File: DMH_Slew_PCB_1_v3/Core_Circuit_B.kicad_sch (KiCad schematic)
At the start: 60 parts, among them J21 Conn_02x03_Top_Bottom, J22 Conn_02x06_Top_Bottom, J23 Conn_02x03_Top_Bottom, J24 Conn_02x03_Top_Bottom, J25 Conn_02x06_Top_Bottom, J26 Conn_02x03_Top_Bottom, J27 Conn_01x08, J28 Conn_01x08, J29 Conn_01x08, J30 Conn_01x08, J6 TS_Jack_6.35mm_Sw, J7 TS_Jack_6.35mm_Sw, J8 TS_Jack_6.35mm_Sw, Q10 BC558, Q7 BC548, Q8 BC548, Q9 BC558, SW4 SW_DPDT_3way, SW5 SW_DPDT, SW6 SPDT_OnOffOn, U3 TL074, U4 TL074

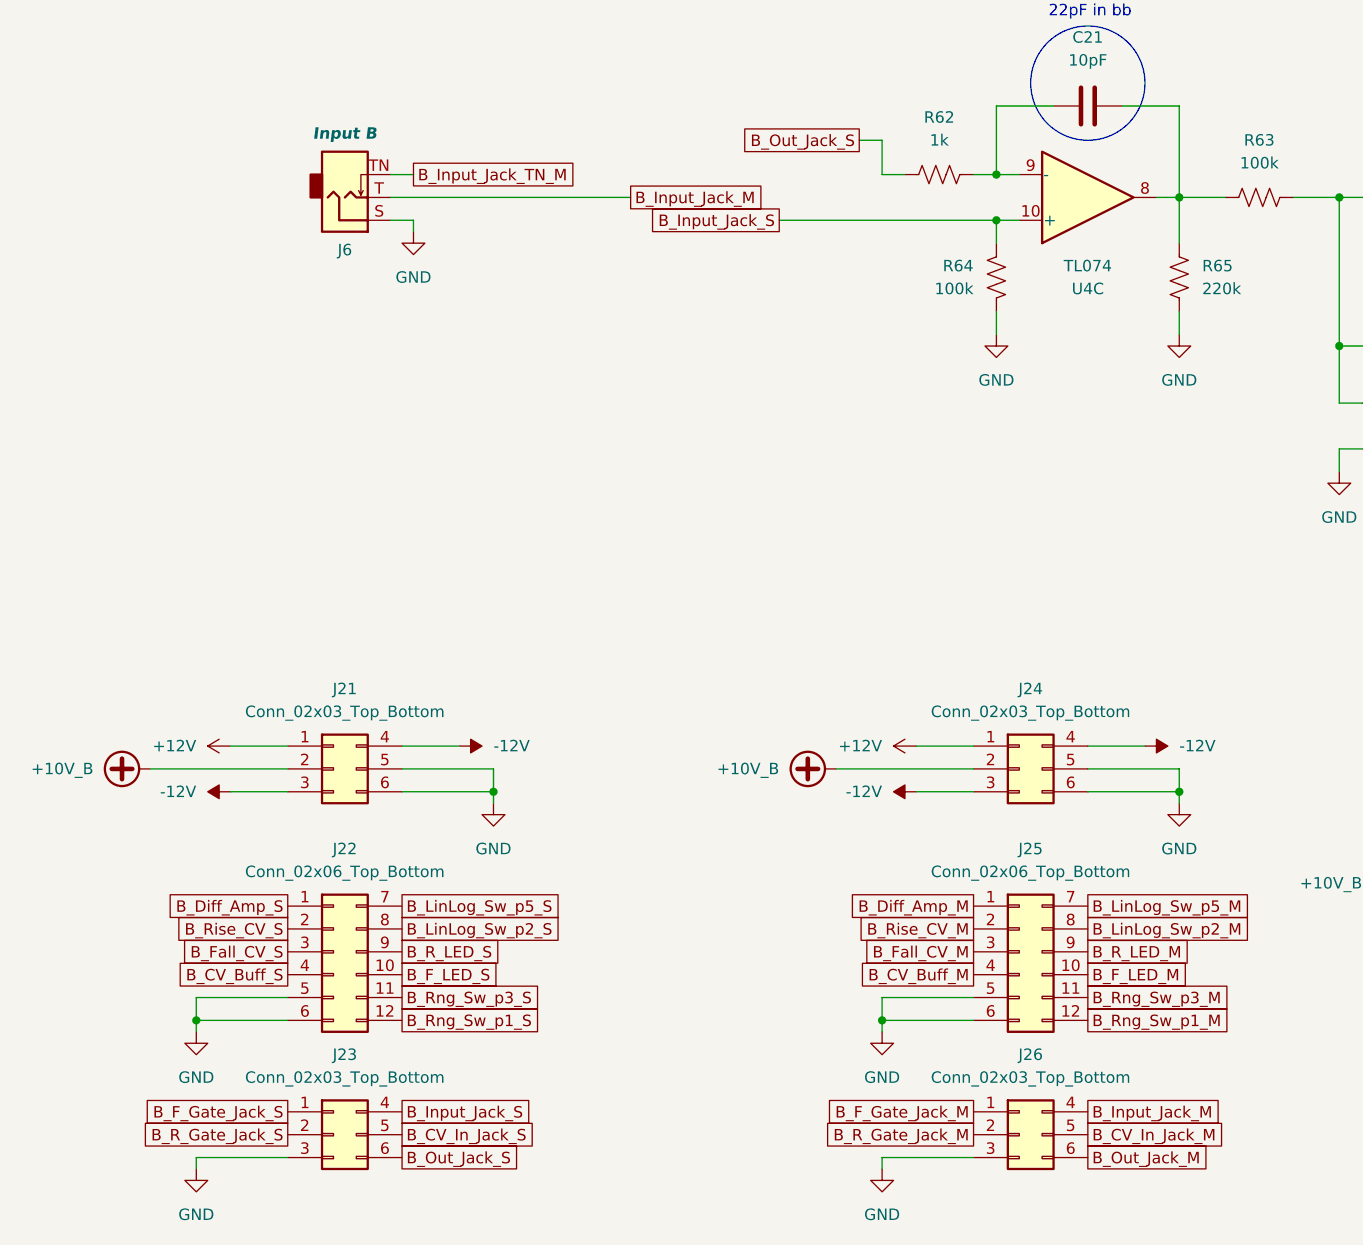
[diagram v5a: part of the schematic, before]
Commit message: Exposed loopback resistor to submodule connector
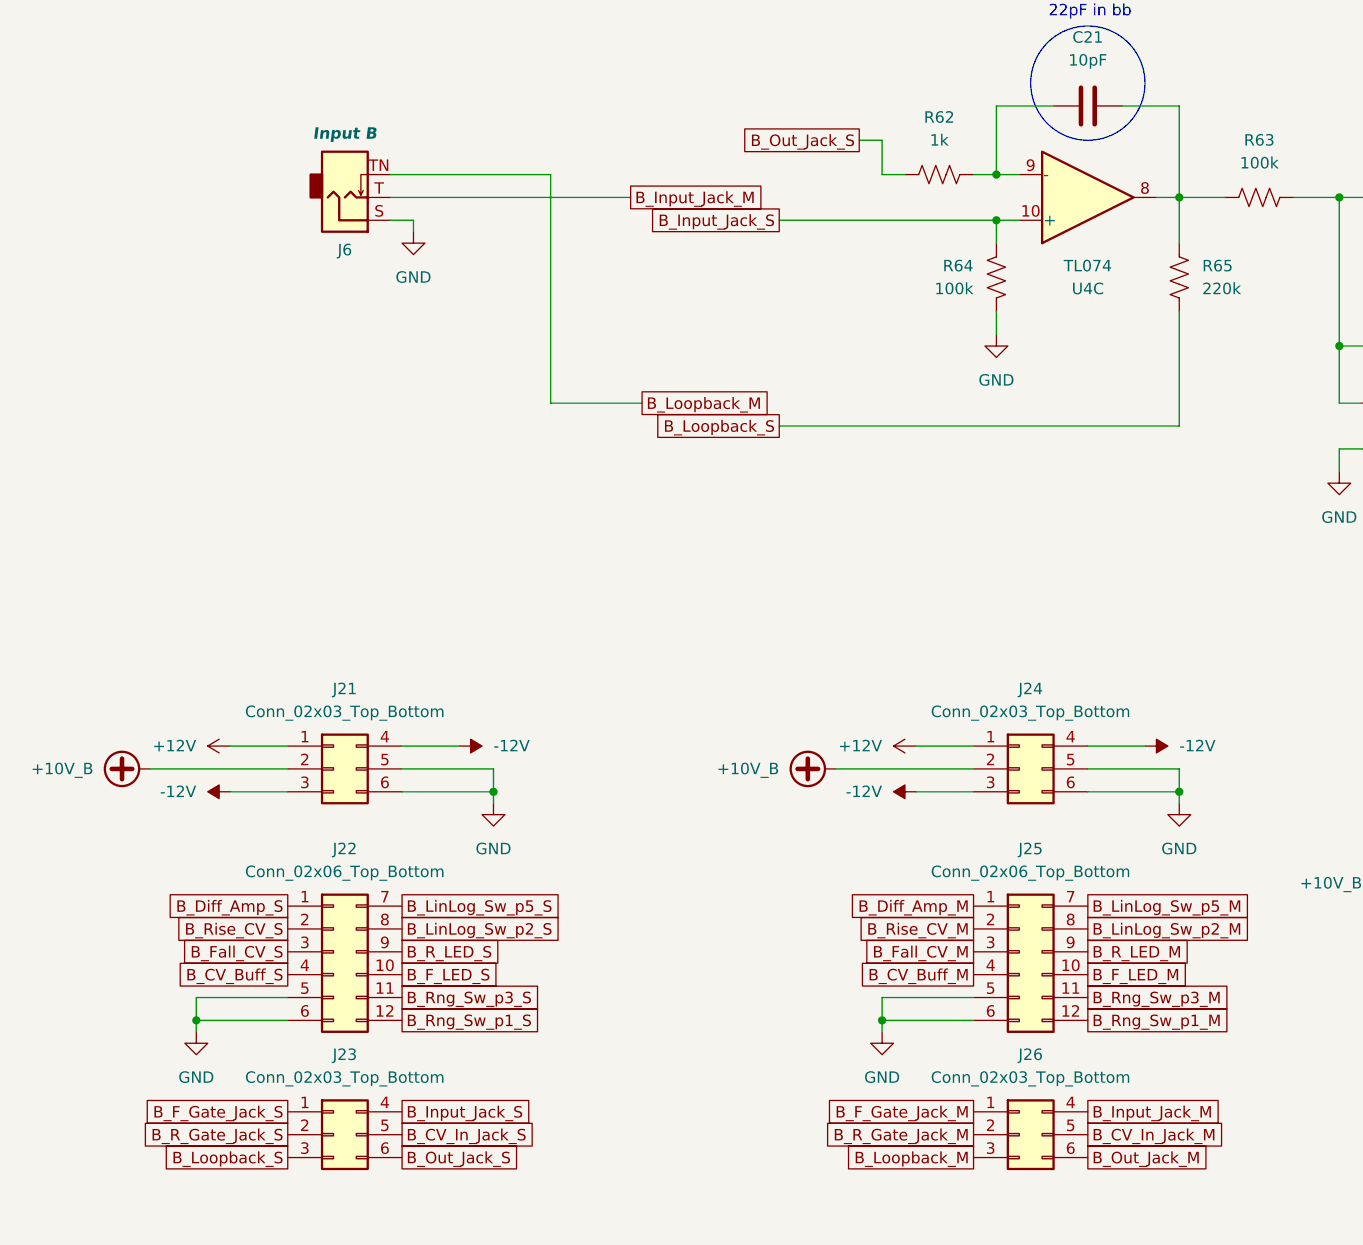
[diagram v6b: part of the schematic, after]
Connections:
- net GND: no longer J23.3 (Pin_3), J26.3 (Pin_3), R65.2
- net B_Input_Jack_TN_M renamed B_Loopback_M
- net B_Loopback_M: now also J26.3 (Pin_3)
- new net B_Loopback_S: J23.3 (Pin_3), R65.2

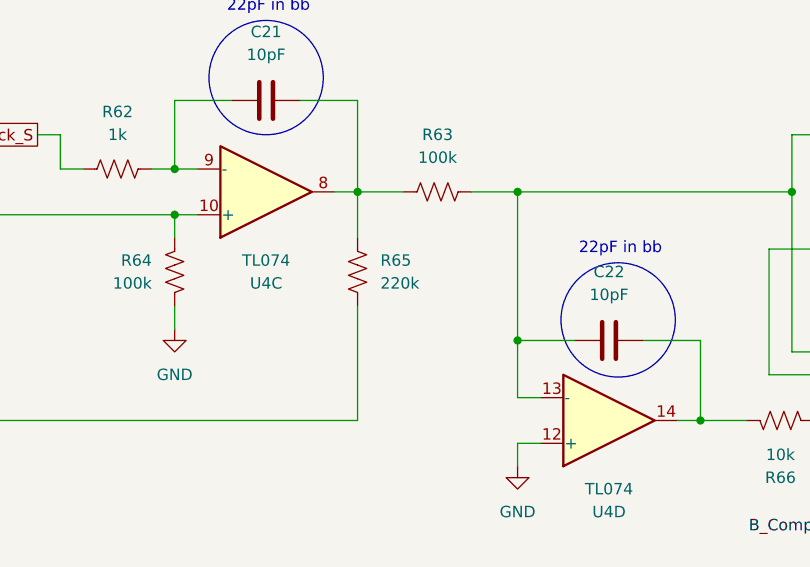
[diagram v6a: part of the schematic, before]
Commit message: Changed loopback resistor to 82k
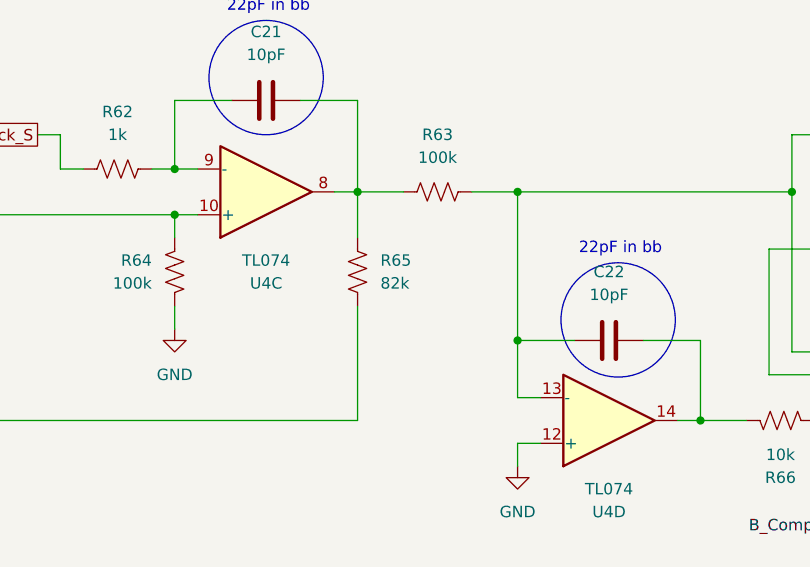
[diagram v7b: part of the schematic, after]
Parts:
- R65: value 220k -> 82k
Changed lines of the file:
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@@
 			)
 		)
-		(property "Value" "220k"
+		(property "Value" "82k"
 			(at 146.05 175.2599 0)
 			(effects

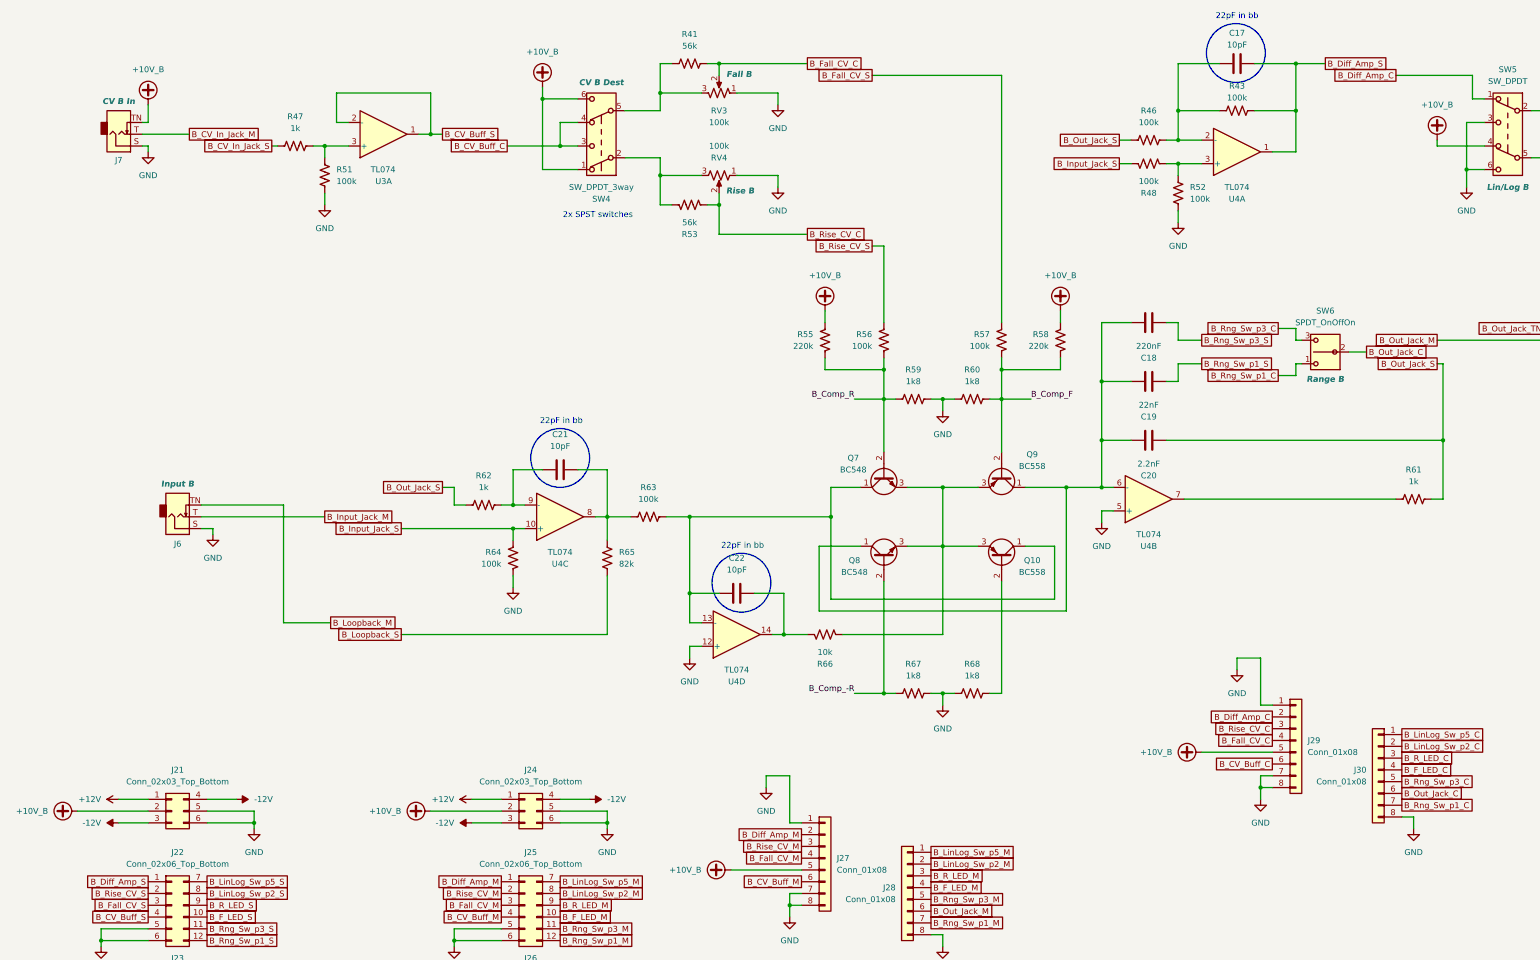
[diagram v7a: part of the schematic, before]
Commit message: Redesigned Main PCB
and regenerated Gerbers
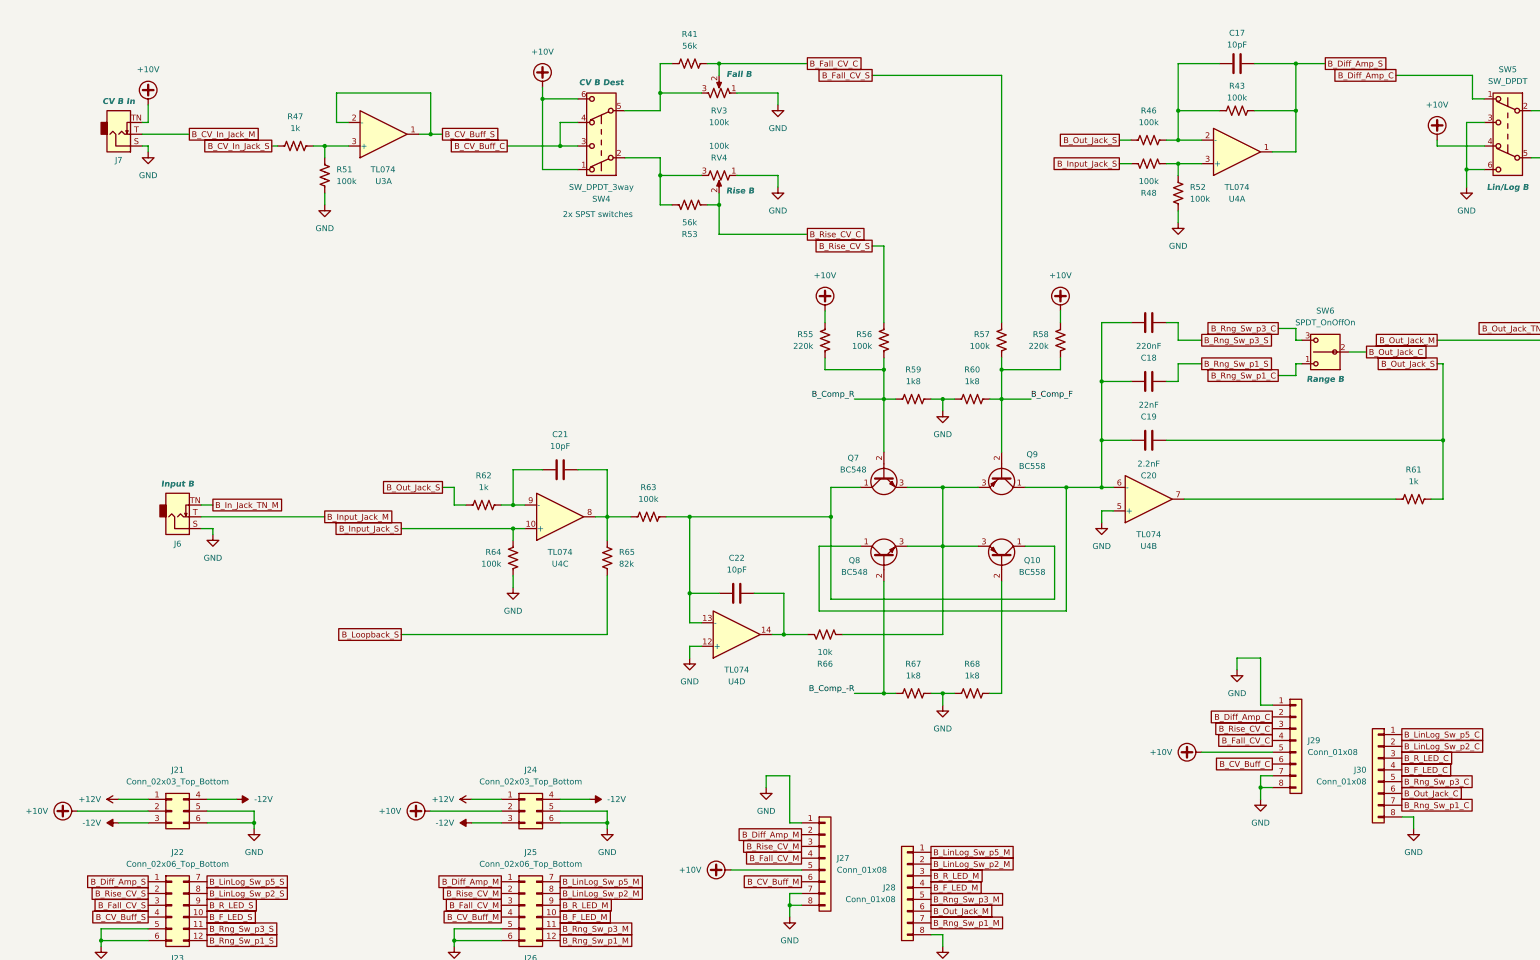
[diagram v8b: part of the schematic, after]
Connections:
- net B_Loopback_M: no longer J6.TN
- net +10V_B renamed +10V
- new net B_In_Jack_TN_M: J6.TN
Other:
- note removed: "22pF in bb"
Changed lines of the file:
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@@
 		(comment 1 "PCB for 5 cm Kosmo format synthesizer module")
 	)
-	(circle
-		(center 279.146 65.024)
-		(radius 6.35)
-		(stroke
-			(width 0)
-			(type default)
-		)
-		(fill
-			(type none)
-		)
-	)
-	(circle
-		(center 172.466 179.324)
-		(radius 6.35)
-		(stroke
-			(width 0)
-			(type default)
-		)
-		(fill
-			(type none)
-		)
-	)
-	(circle
-		(center 133.35 152.4)
-		(radius 6.35)
-		(stroke
-			(width 0)
-			(type default)
-		)
-		(fill
-			(type none)
-		)
-	)
-	(text "22pF in bb"
-		(exclude_from_sim no)
-		(at 172.72 171.45 0)
-		(effects
-			(font
-				(size 1.27 1.27)
-			)
-		)
-	)
-	(text "22pF in bb"
-		(exclude_from_sim no)
-		(at 133.604 144.526 0)
-		(effects
-			(font
-				(size 1.27 1.27)
-			)
-		)
-	)
 	(text "2x SPST switches"
 		(exclude_from_sim no)
@@
 		)
 	)
-	(text "22pF in bb"
-		(exclude_from_sim no)
-		(at 279.4 57.15 0)
-		(effects
-			(font
-				(size 1.27 1.27)
-			)
-		)
-	)
 	(junction
 		(at 228.6 139.7)
@@
 	(wire
 		(pts
-			(xy 73.66 187.96) (xy 83.82 187.96)
-		)
-		(stroke
-			(width 0)
-			(type default)
-		)
-	)
-	(wire
-		(pts
 			(xy 110.49 158.75) (xy 110.49 162.56)
 		)
@@
 	(wire
 		(pts
-			(xy 55.88 162.56) (xy 73.66 162.56)
+			(xy 55.88 162.56) (xy 58.42 162.56)
 		)
 		(stroke
@@
 	(wire
 		(pts
-			(xy 73.66 162.56) (xy 73.66 187.96)
-		)
-		(stroke
-			(width 0)
-			(type default)
-		)
-	)
-	(wire
-		(pts
 			(xy 123.19 167.64) (xy 125.73 167.64)
 		)
@@
 		)
 	)
-	(global_label "B_Loopback_M"
+	(global_label "B_In_Jack_TN_M"
 		(shape passive)
-		(at 83.82 187.96 0)
+		(at 58.42 162.56 0)
 		(fields_autoplaced yes)
 		(effects
@@
 		)
 		(property "Intersheetrefs" "${INTERSHEET_REFS}"
-			(at 99.2403 187.96 0)
+			(at 75.1709 162.56 0)
 			(effects
 				(font
@@
 			)
 		)
-		(property "Value" "+10V_B"
+		(property "Value" "+10V"
 			(at 190.5 113.03 0)
 			(effects
@@
 			)
 		)
-		(property "Value" "+10V_B"
+		(property "Value" "+10V"
 			(at 322.58 76.2 0)
 			(effects
@@
 			)
 		)
-		(property "Value" "+10V_B"
+		(property "Value" "+10V"
 			(at 265.43 215.8999 90)
 			(effects
@@
 			)
 		)
-		(property "Value" "+10V_B"
+		(property "Value" "+10V"
 			(at 163.83 241.2999 90)
 			(effects
@@
 			)
 		)
-		(property "Value" "+10V_B"
+		(property "Value" "+10V"
 			(at 241.3 113.03 0)
 			(effects
@@
 			)
 		)
-		(property "Value" "+10V_B"
+		(property "Value" "+10V"
 			(at 22.86 228.5999 90)
 			(effects
@@
 			)
 		)
-		(property "Value" "+10V_B"
+		(property "Value" "+10V"
 			(at 129.54 64.77 0)
 			(effects
@@
 			)
 		)
-		(property "Value" "+10V_B"
+		(property "Value" "+10V"
 			(at 44.45 68.58 0)
 			(effects
@@
 			)
 		)
-		(property "Value" "+10V_B"
+		(property "Value" "+10V"
 			(at 99.06 228.5999 90)
 			(effects
